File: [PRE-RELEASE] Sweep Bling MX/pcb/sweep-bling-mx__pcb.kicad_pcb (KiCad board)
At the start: 2 copper layers, 113.5 x 95.2 mm, 31 parts, among them J2 AudioJack4dpb, SW10 SW_Push, SW11 SW_Push, SW12 SW_Push, SW14 SW_Push, SW15 SW_Push, SW16 SW_Push, SW17 SW_Push, SW18 SW_Push, SW2 SW_Push, SW20 SW_Push, SW21 SW_Push, SW3 SW_Push, SW4 SW_Push, SW5 SW_Push, SW6 SW_Push, SW8 SW_Push, SW9 SW_Push, U1 ProMicro-kbd

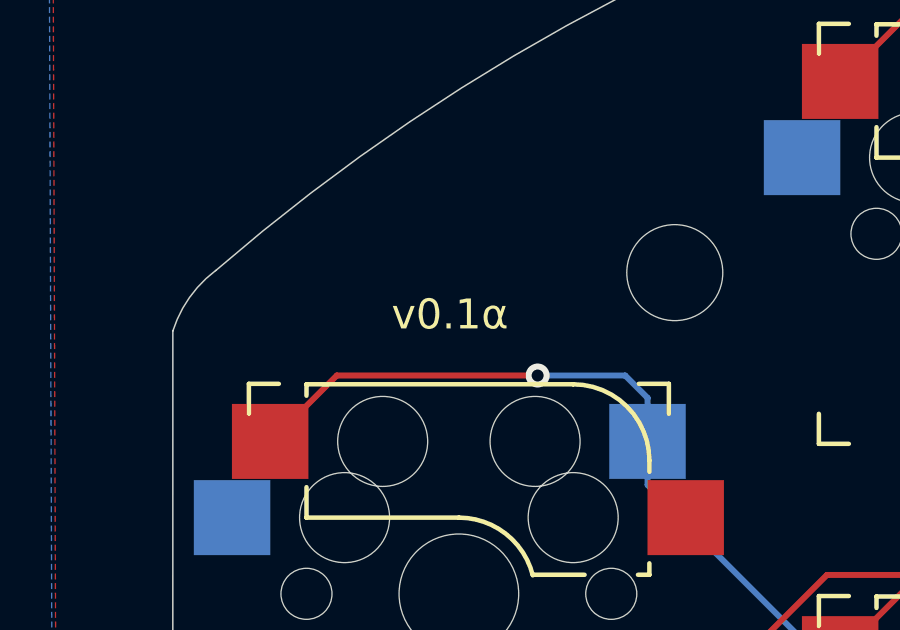
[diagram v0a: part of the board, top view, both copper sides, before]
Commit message: Update version number on PCB (v1.0)
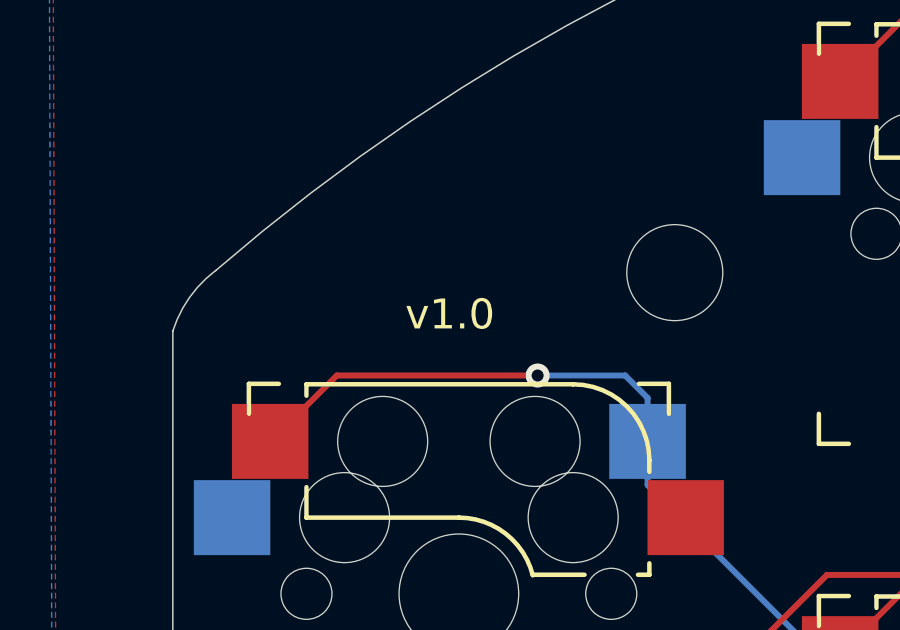
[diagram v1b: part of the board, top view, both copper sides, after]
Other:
- board text added: "v1.0"
- board text removed: "v0.1α"
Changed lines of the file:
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@@
     (effects (font (size 0.6 0.6) (thickness 0.12)) (justify right mirror))
   )
-  (gr_text v0.1α (at 44.704 67.691) (layer F.SilkS)
+  (gr_text v1.0 (at 44.704 67.691) (layer F.SilkS)
     (effects (font (size 1 1) (thickness 0.15)))
   )
